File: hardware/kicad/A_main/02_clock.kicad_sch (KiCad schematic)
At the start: 26 parts, among them U15 ADCLK846BCPZ, U16 SN65LVDS2DBVR, U17 SN65LVDS2DBVR, Y10 ABLNO-V-80.000MHZ

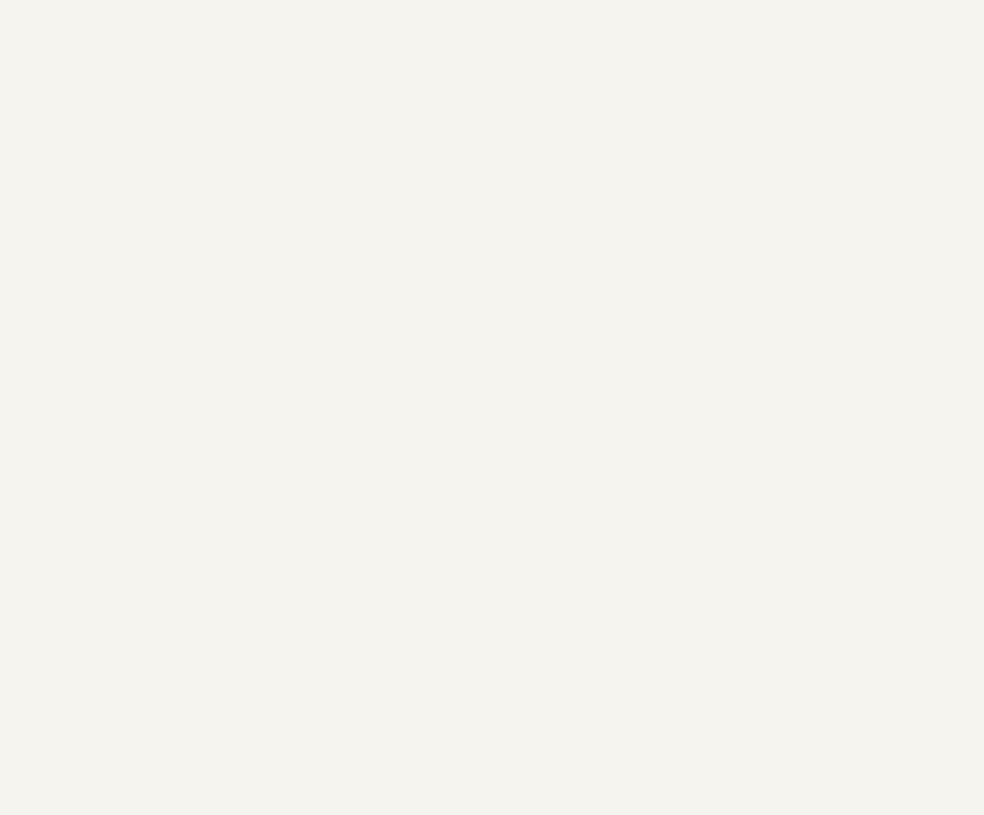
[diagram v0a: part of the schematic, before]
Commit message: Connect the pads that had no net
A symbol pin number must agree with the footprint pad number. If the
numbers do not agree, the net goes nowhere. The netlist removes it
and gives no message. ERC examines the schematic and sees a wire. DRC
does not count an unconnected pad as a violation. All three boards
showed zero ERC violations while 31 pads had no net.

Two of these faults stopped a board.

The footprint of the Ethernet PHY was for a different part. The
project used QFN-48 6x6 mm with 0.4 mm pitch. The RTL8211F(I)-CG is
WQFN-40-EP 5x5 mm. You cannot solder the part to that pad pattern.

The 25 MHz crystal had a 2-pin symbol on a 4-pad footprint. On a 3225
crystal the terminals are the diagonal pads 1 and 3. Pads 2 and 4 are
the metal can. XO went to pad 2. There was no crystal between XI and
XO, and thus neither PHY could make a clock.

The paddle of the AD9251 was pin 0 in the symbol and pad 65 in the
footprint. The paddle of the PE4312 was Pad against pad 21. The gas
discharge tubes had one electrode unconnected, because
Device:GDT_2Pin uses pins 1 and 3 but the varistor footprint uses
pads 1 and 2. A local footprint with pads 1 and 3 corrects this.

ped_denetim.py finds these faults on the board. yap.sh runs it before
the DSN export. The chain stops if a pad has no net.

The DSN export also changed. It declared In1 and In4 as power layers
but did not export the copper on them. The router thus believed that
the two ground planes were empty. It routed the 289 pins of GND as
traces on the signal layers. The planes now go out as conduction
areas.
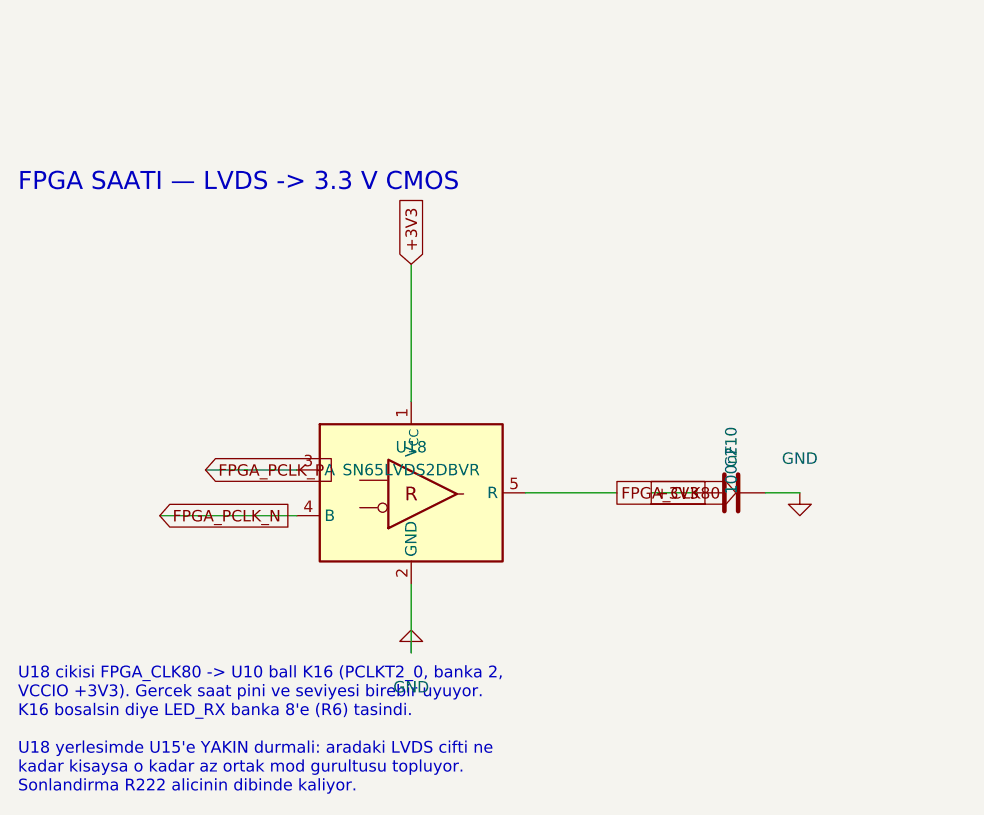
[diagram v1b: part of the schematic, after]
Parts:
- removed C210: 100nF, Capacitor_SMD:C_0603_1608Metric, symbol Device:C
- added C210 (x2): 100nF, Capacitor_SMD:C_0603_1608Metric, symbol Device:C
- added U18: SN65LVDS2DBVR, Package_TO_SOT_SMD:SOT-23-5, symbol Interface:SN65LVDS2DBV
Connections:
- net +3V3: now also C210.1, U18.1 (V_{CC})
- net BUFCLK_P: now also C210.2
- net CLK80_DIV: now also C210.1
- net FPGA_PCLK_N: now also U18.4 (B)
- net FPGA_PCLK_P: now also U18.3 (A)
- net GND: now also C210.2, U18.2 (GND)
- new net FPGA_CLK80: U18.5 (R)
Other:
- note added: "FPGA SAATI — LVDS -> 3.3 V CMOS"
- note added: "U18 cikisi FPGA_CLK80 -> U10 ball K16 (PCLKT2_0, banka 2, VCCIO +3V3). Gercek saat pini ve seviyesi birebir uyuyor. K16 bosalsin diye LED_RX banka 8'e (R6) tasindi. U18 yerlesimde U15'e YAKIN durmali: aradaki LVDS cifti ne kadar kisaysa o kadar az ortak mod gurultusu topluyor. Sonlandirma R222 alicinin dibinde kaliyor."

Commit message: Remove the pads that have no copper from the DSN export
The router reported the same 220 clearance violations in each pass.
At the same time the number of unrouted connections decreased. The
violations were thus in the input and not in the routing.

The -1EP footprints of KiCad put four paste apertures on the exposed
pad. These apertures stop full paste coverage and they have no copper
layer. The DSN export put them on the top copper layer. The image of
U51 in the DSN had 21 pins: 17 correct pins and four unconnected
copper islands in the exposed pad. These islands are always in
conflict with the pad and they close the area below it.

The export now removes a pad that has no copper layer. The image of
U51 has 17 pins. The violations on board D decreased from 220 to 152.
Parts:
- removed C210 (x2): 100nF, Capacitor_SMD:C_0603_1608Metric, symbol Device:C
- added C210 (x2): 100nF, Capacitor_SMD:C_0603_1608Metric, symbol Device:C
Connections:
- net +3V3: now also C210.1
- net BUFCLK_P: now also C210.2
- net CLK80_DIV: now also C210.1
- net GND: now also C210.2

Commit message: Correct the clearance test for the pre-routed traces
The clearance test used a circle for each pad. The radius was
max(width, height)/2. The corner of a rectangle is at
hypot(width, height)/2 from the center. The test thus made the pad
smaller than it is. On the 2.5 x 4.5 mm gate pad of a TO-247 the
difference is 2.250 mm against 2.574 mm.

The DRN_A trace was on the gate pad of Q10 with an overlap of 35 um.
This is a short circuit between the 50 V drain rail and the gate of a
100 W device. The search that finds the tee offset accepted this
route. The overlap is at a corner and 35 um wide. You cannot see it
on a plot.

The test now uses the real shape of the pad and the collision test of
pcbnew. It also uses the 300 um clearance and not only an overlap. A
trace that is 50 um from a pad is also not possible to manufacture.

Board D was built again. No trace is below 300 um and the smallest
gap is 0.537 mm. Boards A and C were correct.
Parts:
- removed C200, C202, C203, C204, C207, C209, C210 (x2), C211, C212: 100nF, Capacitor_SMD:C_0603_1608Metric, symbol Device:C
- removed C201, C205: 10uF, Capacitor_SMD:C_0603_1608Metric, symbol Device:C
- removed FB10: ferrit 600R, Inductor_SMD:L_0603_1608Metric, symbol Device:L
- removed R206, R208, R211, R220, R221, R222, R230: 100R, Resistor_SMD:R_0603_1608Metric, symbol Device:R
- removed R210: 220R, Resistor_SMD:R_0603_1608Metric, symbol Device:R
- removed R212, R213: 1k, Resistor_SMD:R_0603_1608Metric, symbol Device:R
- removed U15: ADCLK846BCPZ, Package_DFN_QFN:HVQFN-24-1EP_4x4mm_P0.5mm_EP2.5x2.5mm_ThermalVias, symbol dogrudan-sdr:ADCLK846
- removed U16, U17, U18: SN65LVDS2DBVR, Package_TO_SOT_SMD:SOT-23-5, symbol Interface:SN65LVDS2DBV
- removed Y10: ABLNO-V-80.000MHZ, dogrudan-sdr:Oscillator_Abracon_ABLNO_4pad_14.3x8.7mm, symbol dogrudan-sdr:ABLNO-V
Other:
- note added: "Saat dagitimi ABLNO-V 80MHz VCXO + ADCLK846 1:6 LVDS fanout Baglantilar: ../NETLIST.md"
- note removed: "** BU BOLUM ILK PLANDA YOKTU. ** VCXO cikisi 3.3 V LVCMOS, ADCLK846 girisinin AZAMI seviyesi 1.8 V p-p (Tablo 1): 'Larger voltage swings can turn on the protection diodes and can degrade jitter performance.' Dogrudan baglansaydi koruma diyotlari iletime girer, jitter bozulurdu — yani aletin manset ozelligi ilk baglantida olurdu. 220R/100R bolucu: 3.3 x 100/320 = 1.03 V p-p. Sinirin altinda. Diren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"
- note removed: "** VS = 1.8 V, 3.3 V DEGIL. ** Veri sayfasinin basligi: '1.8 V, 6 LVDS/12 CMOS Output Clock Fanout Buffer'. Guc agacinda saat bolumu bastan 3.3 V varsayilmisti; tampona kendi +1V8_CLK rayi eklendi (01_power U9, ADP150-1.8, +2V5'ten besleniyor — 3.3'ten dusurmek gereksiz isi uretirdi). Acik ped (25) TOPRAGA, termal via dizisiyle. Veri sayfasi: 'EXPOSED PADDLE MUST BE CONNECTED TO GND.' CTRL_A = CT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"
- note removed: "ADC SAATLERI — LVDS, DOGRUDAN"
- note removed: "ADCLK846 eklemeli jitter (Tablo 1): 54 fs rms 12 kHz - 20 MHz 86 fs rms 10 Hz - 100 MHz 150 fs rms genis bant, 1 V/ns kenar hizinda VCXO 60 fs ile birlikte: dar bant sqrt(60^2 + 54^2) = 81 fs genis bant sqrt(60^2 + 150^2) = 162 fs SNR tavani = -20*log10(2*pi*f*tj): 30 MHz @ 81 fs -> 96 dB ADC'nin kendi SNR'i sinir 500 MHz @ 81 fs -> 72 dB sinirda 500 MHz @ 162 fs -> 66 dB JITTER SINIRLIYOR SONUC: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"
- note removed: "ADCLK846 — 1:6 LVDS"
- note removed: "Alti numarali cikis test icin sonlandirilmis. Bringup'ta osiloskopla saatin gercekten 80 MHz oldugu buradan gorulur — TASARIM.md §11 adim 2. Kart kenarina iki pad."
- note removed: "Besleme gurultusu DOGRUDAN faz gurultusune donusuyor. Kendi LDO'su (01_power U6) + ferrit boncuk + ayri toprak adasi. Olculen: 90.3 fs @50 MHz, 80 MHz'de <100 fs bekleniyor. Vc GPSDO'dan (08_control), DAC ile suruluyor."
- note removed: "DAC SAATLERI — LVDS -> 3.3 V CMOS cevirici"
- note removed: "Dort ADC kanali ve iki DAC ayni saatten besleniyor. Gurultu iptali, yon bulma ve isin sekillendirme bu dagitimin simetrisine bagli."
- note removed: "FPGA SAATI — LVDS -> 3.3 V CMOS"
- note removed: "Her LVDS ciftinin ucunda 100R sonlandirma, ALICIYA yakin. AD9251 saat girisi PECL/LVDS/1.8V CMOS kabul ediyor (Rev.C), cevirici gerekmiyor. ** IKI YOL ES UZUNLUKTA. ** Cikislar arasi skew veri sayfasinda 65 ps (ayni parca uzerinde). Bu SABIT bir fark, kalibre edilebilir; yol uzunlugu farki ise sicaklikla oynar, edilemez."
- note removed: "JITTER BUTCESI — artik tahmin degil"
- note removed: "SAAT DAGITIMI — aletin manset ozelligi bu sayfada"
- note removed: "SN65LVDS2DBVR — LVDS alici, LVTTL cikis, SOT-23-5. LCSC C38204, $0.36, 1244 stok. NETLIST.md §10.2c bu ceviriciyi acik madde birakmisti; kapandi. Neden FPGA'dan uretmedik: FPGA cikis jitter'i ps mertebesinde, verilen sinyalin faz gurultusune dogrudan giriyor. 36 kurusluk parca TX spektrumunu kurtariyor. DAC1_CLK cipin hem CLK1 hem CLK2 bacagina gidiyor (cift port, iki kanal ayni saatte). DAC2 int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"
- note removed: "TEST NOKTASI"
- note removed: "U18 cikisi FPGA_CLK80 -> U10 ball K16 (PCLKT2_0, banka 2, VCCIO +3V3). Gercek saat pini ve seviyesi birebir uyuyor. K16 bosalsin diye LED_RX banka 8'e (R6) tasindi. U18 yerlesimde U15'e YAKIN durmali: aradaki LVDS cifti ne kadar kisaysa o kadar az ortak mod gurultusu topluyor. Sonlandirma R222 alicinin dibinde kaliyor."
- note removed: "VCXO -> TAMPON ARAYUZU — seviye uyumu SART"
- note removed: "VCXO — ABLNO-V, 80.000 MHz"

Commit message: Correct the schematic faults that ERC cannot find
An agent examined the three schematics against the datasheets. ERC
reported zero violations before and after this work. None of these
faults are visible to ERC.

The comparator for the external 10 MHz reference was in shutdown. The
SHDN pin of the TLV3501 went to +3V3. Sixteen DRV8833 devices had VCP
and VINT unconnected. Without the charge pump none of the 28 filter
relays can latch. Seven regulators had no decoupling capacitor within
18 mm to 94 mm. On board D the nearest +12V capacitor to an LM358 was
227 mm away on a 275 mm board.

The PE4312 devices had no series 10k resistor on pin 3. The datasheet
makes this necessary for the attenuation accuracy. Their exposed pad
was 2.6 mm against 2.15 mm. The BOM did not give the load capacitance
of the crystal. This work added 60 parts and changed 4 footprints.

The worst fault was in the tool chain. lib/gen_symbols.py still made
the old pin numbers. The five corrections went into the symbol
library by hand and not into its generator. A new library would have
removed all of them.

The thermal vias are now a decision from the measured clearance and
the dissipation. This work removed them from the PE4312, the RTL8211F
and the ADCLK846. They stay on the DRV8833 and on the LM5164, which
is a 1 W buck converter.

Two checks are new. sema_denetim compares the pin names with the
nets. netlist_denetim locks 22 pin-to-net expectations from the
datasheets and does not need a board.

The boards were built again with these corrections. The chain now
adds the test points: 10 on board A, 7 on board C and 15 on board D.
Each board has 3 fiducials. Every pad has a net.
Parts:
- added C200, C202, C203, C204, C207, C209, C210 (x2), C211, C212: 100nF, Capacitor_SMD:C_0603_1608Metric, symbol Device:C
- added C201, C205: 10uF, Capacitor_SMD:C_0603_1608Metric, symbol Device:C
- added FB10: ferrit 600R, Inductor_SMD:L_0603_1608Metric, symbol Device:L
- added R206, R208, R211, R220, R221, R222, R230: 100R, Resistor_SMD:R_0603_1608Metric, symbol Device:R
- added R210: 220R, Resistor_SMD:R_0603_1608Metric, symbol Device:R
- added R212, R213: 1k, Resistor_SMD:R_0603_1608Metric, symbol Device:R
- added U15: ADCLK846BCPZ, Package_DFN_QFN:HVQFN-24-1EP_4x4mm_P0.5mm_EP2.5x2.5mm, symbol dogrudan-sdr:ADCLK846
- added U16, U17, U18: SN65LVDS2DBVR, Package_TO_SOT_SMD:SOT-23-5, symbol Interface:SN65LVDS2DBV
- added Y10: ABLNO-V-80.000MHZ, dogrudan-sdr:Oscillator_Abracon_ABLNO_4pad_14.3x8.7mm, symbol dogrudan-sdr:ABLNO-V
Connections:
- new net +1V8_CLK: C202.1, C203.1, C204.1, C205.1, U15.10 (VS), U15.13 (VS), U15.16 (VS), U15.19 (VS), U15.22 (VS), U15.4 (VS)
- new net +3V3: C207.1, C209.1, C210.1, U16.1 (V_{CC}), U17.1 (V_{CC}), U18.1 (V_{CC})
- new net +3V3_CLK: FB10.1
- new net ADCLK_U20_N: R220.2, U15.23 (OUT0B)
- new net ADCLK_U20_P: R220.1, U15.24 (OUT0A)
- new net ADCLK_U21_N: R221.2, U15.20 (OUT1B)
- new net ADCLK_U21_P: R221.1, U15.21 (OUT1A)
- new net BUFCLK_N: C211.1, R213.2, U15.2 (CLK-)
- new net BUFCLK_P: C210.2, R212.2, U15.3 (CLK+)
- new net CLK80: R210.1, Y10.3 (OUT)
- new net CLK80_DIV: C210.1, R210.2, R211.1
- new net CLKTEST_N: R230.2, U15.8 (OUT5B)
- new net CLKTEST_P: R230.1, U15.9 (OUT5A)
- new net CLK_VREF: C212.1, R212.1, R213.1, U15.1 (VREF)
- new net DAC1_CLK: U16.5 (R)
- new net DAC2_CLK: U17.5 (R)
- new net DACCLK_LV1_N: R206.2, U15.14 (OUT3B), U16.4 (B)
- new net DACCLK_LV1_P: R206.1, U15.15 (OUT3A), U16.3 (A)
- new net DACCLK_LV2_N: R208.2, U15.11 (OUT4B), U17.4 (B)
- new net DACCLK_LV2_P: R208.1, U15.12 (OUT4A), U17.3 (A)
- new net FPGA_CLK80: U18.5 (R)
- new net FPGA_PCLK_N: R222.2, U15.17 (OUT2B), U18.4 (B)
- new net FPGA_PCLK_P: R222.1, U15.18 (OUT2A), U18.3 (A)
- new net GND: C200.2, C201.2, C202.2, C203.2, C204.2, C205.2, C207.2, C209.2, C210.2, C211.2, C212.2, R211.2, U15.25 (EPAD), U15.5 (CTRL_A), U15.6 (CTRL_B), U15.7 (SLEEP), U16.2 (GND), U17.2 (GND), U18.2 (GND), Y10.2 (GND)
- new net VCXO_VC: Y10.1 (VC)
- new net VCXO_VDD: C200.1, C201.1, FB10.2, Y10.4 (VDD)
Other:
- note added: "** BU BOLUM ILK PLANDA YOKTU. ** VCXO cikisi 3.3 V LVCMOS, ADCLK846 girisinin AZAMI seviyesi 1.8 V p-p (Tablo 1): 'Larger voltage swings can turn on the protection diodes and can degrade jitter performance.' Dogrudan baglansaydi koruma diyotlari iletime girer, jitter bozulurdu — yani aletin manset ozelligi ilk baglantida olurdu. 220R/100R bolucu: 3.3 x 100/320 = 1.03 V p-p. Sinirin altinda. Diren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"
- note added: "** VS = 1.8 V, 3.3 V DEGIL. ** Veri sayfasinin basligi: '1.8 V, 6 LVDS/12 CMOS Output Clock Fanout Buffer'. Guc agacinda saat bolumu bastan 3.3 V varsayilmisti; tampona kendi +1V8_CLK rayi eklendi (01_power U9, ADP150-1.8, +2V5'ten besleniyor — 3.3'ten dusurmek gereksiz isi uretirdi). Acik ped (25) TOPRAGA, termal via dizisiyle. Veri sayfasi: 'EXPOSED PADDLE MUST BE CONNECTED TO GND.' CTRL_A = CT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"
- note added: "ADC SAATLERI — LVDS, DOGRUDAN"
- note added: "ADCLK846 eklemeli jitter (Tablo 1): 54 fs rms 12 kHz - 20 MHz 86 fs rms 10 Hz - 100 MHz 150 fs rms genis bant, 1 V/ns kenar hizinda VCXO 60 fs ile birlikte: dar bant sqrt(60^2 + 54^2) = 81 fs genis bant sqrt(60^2 + 150^2) = 162 fs SNR tavani = -20*log10(2*pi*f*tj): 30 MHz @ 81 fs -> 96 dB ADC'nin kendi SNR'i sinir 500 MHz @ 81 fs -> 72 dB sinirda 500 MHz @ 162 fs -> 66 dB JITTER SINIRLIYOR SONUC: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"
- note added: "ADCLK846 — 1:6 LVDS"
- note added: "Alti numarali cikis test icin sonlandirilmis. Bringup'ta osiloskopla saatin gercekten 80 MHz oldugu buradan gorulur — TASARIM.md §11 adim 2. Kart kenarina iki pad."
- note added: "Besleme gurultusu DOGRUDAN faz gurultusune donusuyor. Kendi LDO'su (01_power U6) + ferrit boncuk + ayri toprak adasi. Olculen: 90.3 fs @50 MHz, 80 MHz'de <100 fs bekleniyor. Vc GPSDO'dan (08_control), DAC ile suruluyor."
- note added: "DAC SAATLERI — LVDS -> 3.3 V CMOS cevirici"
- note added: "Dort ADC kanali ve iki DAC ayni saatten besleniyor. Gurultu iptali, yon bulma ve isin sekillendirme bu dagitimin simetrisine bagli."
- note added: "FPGA SAATI — LVDS -> 3.3 V CMOS"
- note added: "Her LVDS ciftinin ucunda 100R sonlandirma, ALICIYA yakin. AD9251 saat girisi PECL/LVDS/1.8V CMOS kabul ediyor (Rev.C), cevirici gerekmiyor. ** IKI YOL ES UZUNLUKTA. ** Cikislar arasi skew veri sayfasinda 65 ps (ayni parca uzerinde). Bu SABIT bir fark, kalibre edilebilir; yol uzunlugu farki ise sicaklikla oynar, edilemez."
- note added: "JITTER BUTCESI — artik tahmin degil"
- note added: "SAAT DAGITIMI — aletin manset ozelligi bu sayfada"
- note added: "SN65LVDS2DBVR — LVDS alici, LVTTL cikis, SOT-23-5. LCSC C38204, $0.36, 1244 stok. NETLIST.md §10.2c bu ceviriciyi acik madde birakmisti; kapandi. Neden FPGA'dan uretmedik: FPGA cikis jitter'i ps mertebesinde, verilen sinyalin faz gurultusune dogrudan giriyor. 36 kurusluk parca TX spektrumunu kurtariyor. DAC1_CLK cipin hem CLK1 hem CLK2 bacagina gidiyor (cift port, iki kanal ayni saatte). DAC2 int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"
- note added: "TEST NOKTASI"
- note added: "U18 cikisi FPGA_CLK80 -> U10 ball K16 (PCLKT2_0, banka 2, VCCIO +3V3). Gercek saat pini ve seviyesi birebir uyuyor. K16 bosalsin diye LED_RX banka 8'e (R6) tasindi. U18 yerlesimde U15'e YAKIN durmali: aradaki LVDS cifti ne kadar kisaysa o kadar az ortak mod gurultusu topluyor. Sonlandirma R222 alicinin dibinde kaliyor."
- note added: "VCXO -> TAMPON ARAYUZU — seviye uyumu SART"
- note added: "VCXO — ABLNO-V, 80.000 MHz"
- note removed: "Saat dagitimi ABLNO-V 80MHz VCXO + ADCLK846 1:6 LVDS fanout Baglantilar: ../NETLIST.md"

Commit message: Move each decoupling capacitor to the pin it serves
The audit found 14 chips with no decoupling capacitor within 15 mm.
Across the boards the nearest capacitor to a supply rail was a median
7.5 mm on A and 6.3 mm on C, and 91 mm in the worst case. A capacitor
45 mm from its pin has about 45 nH of loop inductance, near 2.8 ohm at
10 MHz, where milliohms are necessary. It is on the schematic, it is
in the BOM, it is fitted, and it does nothing.

The pass that moves capacitors ran before the fallback placer, so a
chip with no explicit rule was not yet placed and never entered the
pool. The fallback then gave every spare capacitor to the chip with
the most pins on the rail, which is the FPGA on +3V3. Small parts got
none. The pass now runs last.

A count of missing parts was also wrong. Every pad on a rail was
counted as a supply pin, including logic inputs tied high: SRCLR on
the 74HC595, SLEEP on the DRV8833, P/S on the PE4312. Counting only
pins the netlist marks power_in, board C has 15 supply pins and 15
capacitors. Four capacitors are missing across all three boards, not
59. The AD8318 has three supply pins and had one capacitor; it now
has three. The ADCLK846 has six and had five.
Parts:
- removed C207, C209, C210 (x2), C211: 100nF, Capacitor_SMD:C_0603_1608Metric, symbol Device:C
- removed R206, R208: 100R, Resistor_SMD:R_0603_1608Metric, symbol Device:R
- added C206: 10uF, Capacitor_SMD:C_0603_1608Metric, symbol Device:C
- added C208, C210 (x2), C211 (x2): 100nF, Capacitor_SMD:C_0603_1608Metric, symbol Device:C
- added R207, R209: 100R, Resistor_SMD:R_0603_1608Metric, symbol Device:R
- C205: value 10uF -> 100nF
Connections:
- net +1V8_CLK: now also C206.1
- net +3V3: now also C208.1, C210.1, C211.1
- net BUFCLK_N: now also C211.1
- net BUFCLK_P: now also C210.2
- net CLK80_DIV: now also C210.1
- net DACCLK_LV1_N: now also R207.2
- net DACCLK_LV1_P: now also R207.1
- net DACCLK_LV2_N: now also R209.2
- net DACCLK_LV2_P: now also R209.1
- net GND: now also C206.2, C208.2, C210.2, C211.2, C211.2

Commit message: Do not count a bulk capacitor as decoupling
The placement pass accepted any capacitor on the rail as sufficient.
On board A the flash memory had 10 uF at 5.5 mm and 47 uF at 16.3 mm,
so the pass was satisfied. Both are bulk. The nearest 100 nF was
17.0 mm away, and at that distance the loop inductance removes the
reason to fit it.

The audit tool already used a 10 uF ceiling for this. The placer did
not, so the two disagreed, and the placer was wrong.

The pass now treats only capacitors of 1 uF and below as decoupling,
both when it asks whether a pin is served and when it selects one to
move. It also searches a ring around the pin for free space instead
of using a fixed offset.

Findings fall from 14 to 4. Board A is clean.

Also: build.sh never ran bom.py, so BOM_*.csv were hand-made files
that no step regenerated and the BOM no longer matched the schematic.
Each board's build now writes its own.
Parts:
- removed C210 (x2), C211 (x2): 100nF, Capacitor_SMD:C_0603_1608Metric, symbol Device:C
- added C210 (x2), C211 (x2): 100nF, Capacitor_SMD:C_0603_1608Metric, symbol Device:C
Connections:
- net +3V3: now also C210.1, C211.1
- net BUFCLK_N: now also C211.1
- net BUFCLK_P: now also C210.2
- net CLK80_DIV: now also C210.1
- net GND: now also C210.2, C211.2, C211.2
